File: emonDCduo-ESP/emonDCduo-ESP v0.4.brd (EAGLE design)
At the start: 99.1 x 76.5 mm, 78 parts, among them Q1 16Mhz XT49M-2016M, U1_TQFP ATMEGA328P

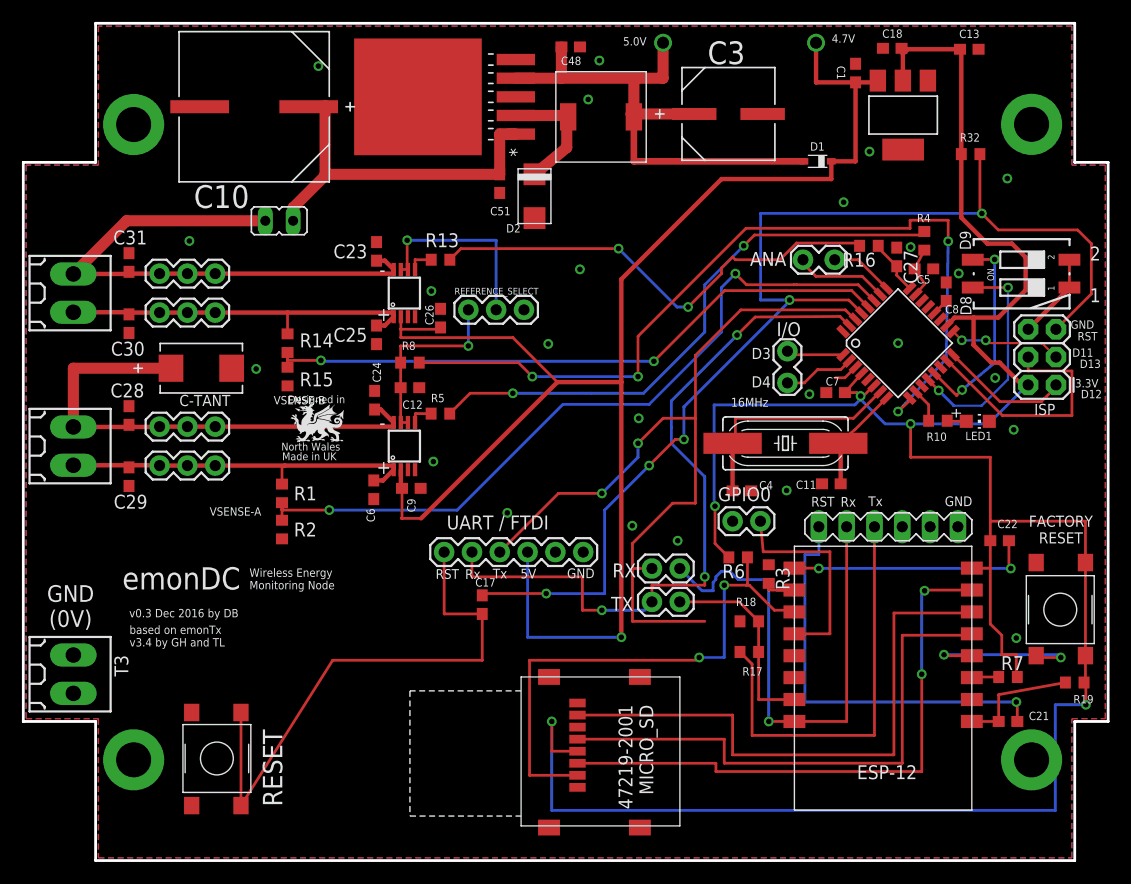
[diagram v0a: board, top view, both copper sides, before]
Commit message: RFM69 onto board
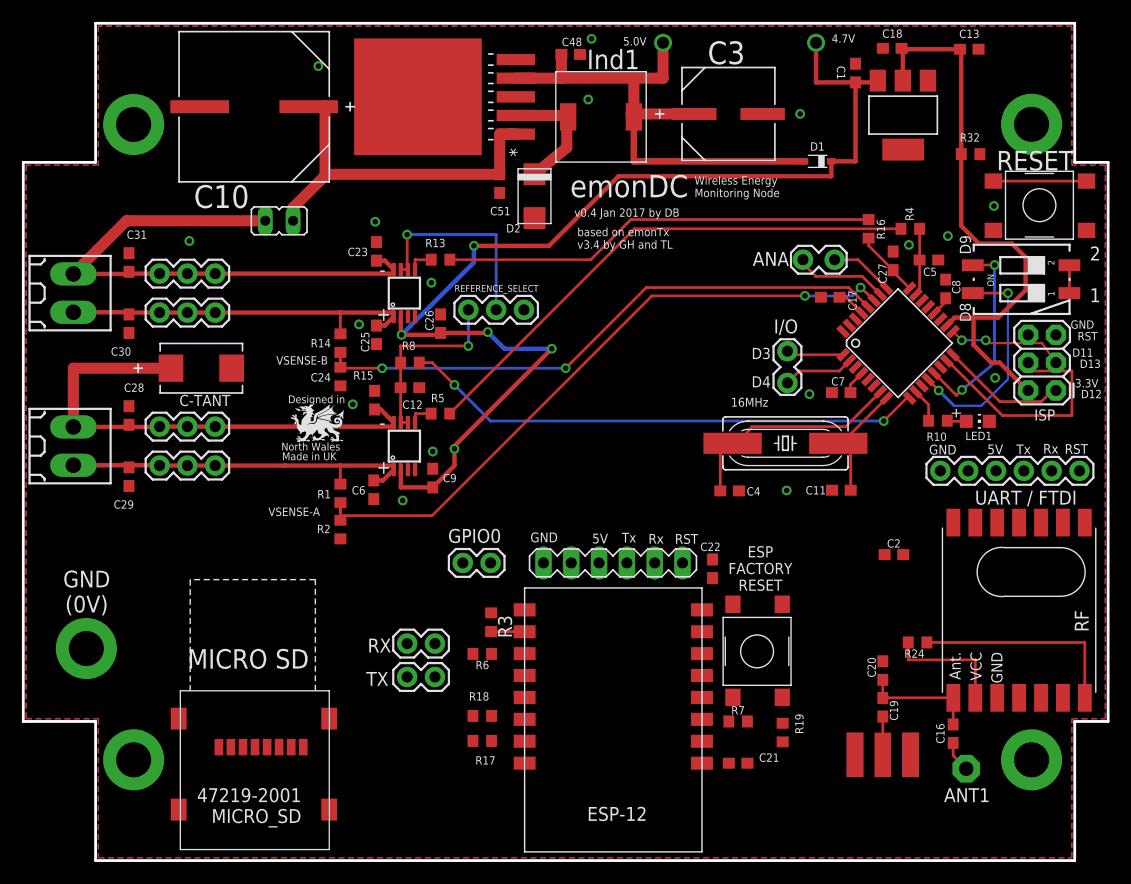
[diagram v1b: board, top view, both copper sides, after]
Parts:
- removed T3: (no value), con-weidmueller-sl35:180-2
- added ANT1: (no value), discrete:PAD-01
- added C16, C19: 22pF, rcl:C0603
- added C2: 100nF, rcl:C0603
- added C20: tune, rcl:C0603
- added J$1: SMA_EDGE, SparkFun-Connectors:SMA-EDGE
- added R24: 120K, rcl:R0603
- added RF: RFM12B, JeeParts:RFM12B
- C3: value 470UF -> 470uF
- moved MC32882 87.2 mm to (89.9, 58.5), turned to 0 degrees
- moved FTDI/UART 58.5 mm to (96.7, 37.4), turned to 180 degrees
- moved C17 42.4 mm to (73.9, 53.2), turned to 0 degrees
- moved MC1 27.9 mm to (70.4, 17.8)
- moved R19 27.1 mm to (69.6, 13.5), turned to 90 degrees
- moved C22 26.3 mm to (63.2, 28.4), turned to 270 degrees
- moved R18 25.9 mm to (42.2, 15.0)
- moved R3 25.7 mm to (43.0, 23.5)
- moved R17 25.7 mm to (42.2, 12.7)
- moved R6 25.0 mm to (42.2, 20.7)
- moved R7 25.0 mm to (65.5, 14.5)
- moved C21 24.9 mm to (65.5, 10.7)
- moved ESP-12 24.9 mm to (62.2, 26.7)
- moved GPIO0 24.9 mm to (40.4, 29.0)
- moved RX 23.4 mm to (37.8, 21.6)
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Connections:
- new net DIG1: C16.1, C19.1, C20.1, RF.ANT
- new net N$11: ANT1.1, C16.2
- new net N$24: C19.2, J$1.SIG
- net 3.3V: now also C2.1, R24.2, RF.VDD
- net D10: now also R24.1, RF.SEL
- net D11/MOSI: now also RF.SDI
- net D12/MISO: now also RF.SDO
- net D13/SCK: now also RF.SCK
- net D2: now also RF.IRQ
- net GND: now also C2.2, C20.2, J$1.GND@0, J$1.GND@1, J$1.GND@2, J$1.GND@3, RF.GND, RF.P$12; no longer T3.1, T3.2
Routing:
- net 3.3V: track 235.1 -> 66.2 mm, vias 5 -> 0
- net RESET: track 109.5 -> 2.63 mm, vias 5 -> 0
- net D0/RX: track 76.7 -> 0.00 mm, vias 2 -> 0
- net D1/TX: track 66.3 -> 0.00 mm, vias 3 -> 0
- net GPIO13: track 53.3 -> 0.00 mm, vias 2 -> 0
- net GPIO12: track 52.7 -> 0.00 mm
- net GPIO14: track 50.0 -> 0.00 mm
- net GPIO2: track 49.5 -> 0.00 mm, vias 2 -> 0
- net ESPTX: track 48.5 -> 0.00 mm, vias 1 -> 0
- net 4.7V: track 148.1 -> 104.2 mm, vias 2 -> 6
- net RES: track 52.0 -> 9.26 mm
- net N$30: track 38.4 -> 0.00 mm, vias 1 -> 0
- net N$36: track 38.3 -> 0.00 mm
- net D5/PWM0: track 78.3 -> 48.0 mm, vias 4 -> 2
- net GPIO15: track 27.1 -> 4.69 mm, vias 2 -> 0
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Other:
- board text added: "ESP FACTORY RESET"
- board text added: "Ind1"
- board text added: "MICRO SD"
- board text added: "v0.4 Jan 2017 by DB"
- board text removed: "FACTORY RESET"
- board text removed: "v0.3 Dec 2016 by DB"

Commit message: layout changes
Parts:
- moved RX 7.41 mm to (37.1, 14.2)
- moved ANA 1.78 mm to (72.4, 56.6)
- moved TX 1.70 mm to (37.1, 17.0)
- moved GPIO0 1.63 mm to (41.7, 27.9)
- moved FTDI/UART 1.27 mm to (95.4, 37.4)
- moved C2 0.51 mm to (79.8, 30.2)
- moved C17 0.34 mm to (73.9, 52.9)
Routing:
- net 3.3V: track 66.2 -> 269.4 mm, vias 0 -> 6
- net D0/RX: track 0.00 -> 93.7 mm, vias 0 -> 3
- net D1/TX: track 0.00 -> 86.1 mm, vias 0 -> 4
- net 4.7V: track 104.2 -> 167.9 mm, vias 6 -> 8
- net GPIO13: track 0.00 -> 63.0 mm, vias 0 -> 2
- net RES: track 9.26 -> 64.3 mm, vias 0 -> 3
- net GPIO14: track 0.00 -> 54.8 mm
- net GPIO12: track 0.00 -> 52.5 mm
- net GPIO2: track 0.00 -> 50.5 mm, vias 0 -> 2
- net D10: track 19.6 -> 67.7 mm, vias 0 -> 4
- net RESET: track 2.63 -> 49.1 mm, vias 0 -> 2
- net ESPTX: track 0.00 -> 42.7 mm, vias 0 -> 1
- net D2: track 0.00 -> 41.3 mm, vias 0 -> 2
- net D13/SCK: track 11.0 -> 45.2 mm, vias 2 -> 5
- net N$36: track 0.00 -> 33.7 mm, vias 0 -> 1
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
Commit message: DRC edited
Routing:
- net GPIO13: track 63.0 -> 64.9 mm
- net D12/MISO: track 26.4 -> 27.9 mm
- net GPIO2: track 50.5 -> 50.0 mm
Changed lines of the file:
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@@
 <rectangle x1="50.109509375" y1="16.957528125" x2="52.101309375" y2="19.025528125" layer="122" rot="R180"/>
 <text x="74.295" y="17.145" size="1.778" layer="112" font="vector" ratio="10"></text>
-<text x="50.5642" y="60.5648" size="0.762" layer="112" font="vector" ratio="15">v0.4 Jan 2017 by DB</text>
-<text x="50.1844" y="62.343" size="2.032" layer="112" font="vector" ratio="15">emonDC</text>
+<text x="10.4322" y="26.5288" size="0.762" layer="112" font="vector" ratio="15">v0.4 Jan 2017 by DB</text>
+<text x="10.0524" y="28.307" size="2.032" layer="112" font="vector" ratio="15">emonDC</text>
 <text x="26.2382" y="12.0142" size="1.016" layer="22" font="vector" ratio="15" rot="MR0">Open-Hardware</text>
 <text x="24.432340625" y="43.539921875" size="0.7112" layer="121" font="vector" ratio="15" rot="SR0">Designed in </text>
@@
 <rectangle x1="91.710159375" y1="63.837721875" x2="91.805359375" y2="63.844121875" layer="22" rot="R180"/>
 <rectangle x1="91.297359375" y1="63.837721875" x2="91.341859375" y2="63.844121875" layer="22" rot="R180"/>
-<text x="61.5446" y="62.3594" size="0.762" layer="112" font="vector" ratio="15">Wireless Energy
+<text x="21.4126" y="28.3234" size="0.762" layer="112" font="vector" ratio="15">Wireless Energy
 Monitoring Node</text>
 <text x="62.865" y="33.401" size="1.4224" layer="122" rot="MR0">SMT V0.6 rev3</text>
@@
 <wire x1="6.858" y1="78.232" x2="96.266" y2="78.232" width="0.254" layer="20"/>
 <wire x1="100" y1="80" x2="100" y2="0" width="0.05" layer="157"/>
-<text x="50.8428" y="57.6492" size="0.762" layer="112" font="vector" ratio="15">based on emonTx
+<text x="10.7108" y="23.6132" size="0.762" layer="112" font="vector" ratio="15">based on emonTx
 v3.4 by GH and TL</text>
 <text x="74.0766" y="76.4598" size="0.762" layer="112" font="vector" ratio="15">4.7V</text>
@@
 <via x="86.7134" y="29.3402" extent="1-16" drill="0.5"/>
 <via x="80.1602" y="49.0252" extent="1-16" drill="0.5"/>
+<wire x1="28.194" y1="6.432" x2="28.304" y2="11.442" width="0" layer="19" extent="1-1"/>
 </signal>
 <signal name="ADCVSENSE-A">
@@
 <wire x1="95.25" y1="35.306" x2="81.28" y2="35.306" width="0.254" layer="16"/>
 <wire x1="81.28" y1="35.306" x2="81.28" y2="40.386" width="0.254" layer="16"/>
-<wire x1="81.28" y1="40.386" x2="72.898" y2="49.022" width="0.254" layer="16"/>
-<via x="72.898" y="49.022" extent="1-16" drill="0.5"/>
-<wire x1="72.898" y1="49.022" x2="73.953425" y2="50.077425" width="0.254" layer="1"/>
+<wire x1="81.28" y1="40.386" x2="72.7456" y2="48.9204" width="0.254" layer="16"/>
+<via x="72.7456" y="48.9204" extent="1-16" drill="0.5"/>
+<wire x1="72.7456" y1="48.9204" x2="73.953425" y2="50.077425" width="0.254" layer="1"/>
 <wire x1="73.953425" y1="50.077425" x2="75.121771875" y2="50.077425" width="0.254" layer="1"/>
 </signal>
@@
 <wire x1="84.5865375" y1="47.400884375" x2="84.552115625" y2="47.400884375" width="0.2032" layer="1"/>
 <wire x1="84.552115625" y1="47.400884375" x2="84.5312" y2="47.4726" width="0.2032" layer="1"/>
-<wire x1="92.012" y1="47.244" x2="92.012" y2="46.482" width="0.254" layer="1"/>
-<wire x1="92.012" y1="46.482" x2="96.012" y2="46.482" width="0.254" layer="1"/>
+<wire x1="92.012" y1="47.244" x2="92.012" y2="45.9994" width="0.254" layer="1"/>
+<wire x1="92.012" y1="45.9994" x2="96.012" y2="45.9994" width="0.254" layer="1"/>
 <wire x1="84.5865375" y1="47.400884375" x2="84.679115625" y2="47.400884375" width="0.254" layer="1"/>
 <wire x1="84.679115625" y1="47.400884375" x2="89.662" y2="42.418" width="0.254" layer="1"/>
 <wire x1="89.662" y1="42.418" x2="94.996" y2="42.418" width="0.254" layer="1"/>
 <wire x1="94.996" y1="42.418" x2="96.012" y2="42.418" width="0.254" layer="1"/>
-<wire x1="96.012" y1="42.418" x2="96.012" y2="46.482" width="0.254" layer="1"/>
+<wire x1="96.012" y1="42.418" x2="96.012" y2="45.9994" width="0.254" layer="1"/>
 <contactref element="RF" pad="SDI"/>
 <wire x1="93.186" y1="16.638" x2="93.218" y2="16.67" width="0.254" layer="1"/>
@@
 <contactref element="ISP" pad="1"/>
 <wire x1="85.1052625" y1="48.038934375" x2="85.152225" y2="47.966571875" width="0.2032" layer="1"/>
-<wire x1="85.152225" y1="47.966571875" x2="89.430796875" y2="43.688" width="0.254" layer="1"/>
-<wire x1="89.430796875" y1="43.688" x2="93.218" y2="43.688" width="0.254" layer="1"/>
-<wire x1="93.218" y1="43.688" x2="94.552" y2="45.022" width="0.254" layer="1"/>
+<wire x1="85.152225" y1="47.966571875" x2="89.938796875" y2="43.18" width="0.254" layer="1"/>
+<wire x1="89.938796875" y1="43.18" x2="94.5642" y2="43.18" width="0.254" layer="1"/>
+<wire x1="94.5642" y1="43.18" x2="94.552" y2="45.022" width="0.254" layer="1"/>
 <wire x1="94.552" y1="45.022" x2="94.552" y2="44.704" width="0.254" layer="1"/>
 <contactref element="RF" pad="SDO"/>
@@
 <via x="88.141" y="49.284" extent="1-16" drill="0.5"/>
 <wire x1="88.141" y1="49.284" x2="88.259" y2="49.029" width="0.2032" layer="1"/>
-<wire x1="88.259" y1="49.029" x2="88.206" y2="49.032" width="0.2032" layer="1"/>
-<wire x1="88.206" y1="49.032" x2="93.282" y2="49.022" width="0.2032" layer="1"/>
-<wire x1="93.282" y1="49.022" x2="94.552" y2="47.244" width="0.2032" layer="1"/>
+<wire x1="88.259" y1="49.029" x2="88.7394" y2="48.524" width="0.2032" layer="1"/>
+<wire x1="88.7394" y1="48.524" x2="93.8154" y2="48.514" width="0.2032" layer="1"/>
+<wire x1="93.8154" y1="48.514" x2="94.552" y2="47.244" width="0.2032" layer="1"/>
 <wire x1="85.1052625" y1="49.9796625" x2="85.152225" y2="50.077425" width="0.2032" layer="1"/>
 <contactref element="RF" pad="SCK"/>
@@
 <wire x1="82.1042" y1="59.4664" x2="82.1042" y2="56.6238" width="0.254" layer="1"/>
 <wire x1="82.1042" y1="56.6238" x2="82.1002" y2="56.6198" width="0.254" layer="1"/>
-<wire x1="82.1002" y1="56.6198" x2="82.1002" y2="53.813625" width="0.254" layer="1"/>
-<wire x1="82.1002" y1="53.813625" x2="81.7581125" y2="53.4715375" width="0.254" layer="1"/>
+<wire x1="82.296" y1="54.009425" x2="81.7581125" y2="53.4715375" width="0.254" layer="1"/>
+<wire x1="82.296" y1="54.009425" x2="82.296" y2="56.6198" width="0.254" layer="1"/>
+<wire x1="82.296" y1="56.6198" x2="82.1002" y2="56.6198" width="0.254" layer="1"/>
 </signal>
 <signal name="N$6">
@@
 <contactref element="U1_TQFP" pad="9"/>
 <wire x1="81.0692625" y1="44.155334375" x2="81.192425" y2="44.006771875" width="0.2032" layer="1"/>
-<wire x1="81.0692625" y1="44.155334375" x2="78.823928125" y2="41.91" width="0.254" layer="1"/>
-<wire x1="78.823928125" y1="41.91" x2="42.926" y2="41.91" width="0.254" layer="16"/>
+<wire x1="81.0692625" y1="44.155334375" x2="78.671528125" y2="41.8084" width="0.254" layer="1"/>
+<wire x1="78.671528125" y1="41.8084" x2="42.926" y2="41.91" width="0.254" layer="16"/>
 <wire x1="42.926" y1="41.91" x2="39.624" y2="45.212" width="0.254" layer="16"/>
 <via x="39.624" y="45.212" extent="1-16" drill="0.5"/>
 <wire x1="39.624" y1="45.212" x2="37.592" y2="47.244" width="0.254" layer="1"/>
 <wire x1="37.592" y1="47.244" x2="36.41" y2="47.244" width="0.254" layer="1"/>
-<via x="78.823928125" y="41.91" extent="1-16" drill="0.5"/>
+<via x="78.671528125" y="41.8084" extent="1-16" drill="0.5"/>
 </signal>
 <signal name="N$19">
@@
 <contactref element="U$1" pad="PIN2"/>
 <contactref element="R6" pad="1"/>
-<wire x1="19.214" y1="12.132" x2="19.214" y2="4.572" width="0.254" layer="1"/>
-<wire x1="19.214" y1="4.572" x2="42.926" y2="4.572" width="0.254" layer="1"/>
-<via x="42.926" y="4.572" extent="1-16" drill="0.5"/>
-<wire x1="42.926" y1="4.572" x2="42.926" y2="18.034" width="0.254" layer="16"/>
+<wire x1="19.214" y1="12.132" x2="19.214" y2="4.826" width="0.254" layer="1"/>
+<via x="42.926" y="6.604" extent="1-16" drill="0.5"/>
+<wire x1="42.926" y1="6.604" x2="42.926" y2="18.034" width="0.254" layer="16"/>
 <via x="42.926" y="18.034" extent="1-16" drill="0.5"/>
 <wire x1="42.926" y1="18.034" x2="42.926" y2="20.6502" width="0.254" layer="1"/>
@@
 <wire x1="43.014" y1="20.6502" x2="43.0338" y2="20.67" width="0.254" layer="1"/>
 <wire x1="43.0338" y1="20.67" x2="46.03" y2="20.67" width="0.254" layer="1"/>
+<wire x1="42.926" y1="6.604" x2="42.926" y2="4.826" width="0.254" layer="1"/>
+<wire x1="42.926" y1="4.826" x2="19.214" y2="4.826" width="0.254" layer="1"/>
 </signal>
 <signal name="GPIO5">
@@
 <wire x1="20.314" y1="6.858" x2="25.908" y2="6.858" width="0.254" layer="1"/>
 <via x="25.908" y="6.858" extent="1-16" drill="0.5"/>
-<wire x1="25.908" y1="6.858" x2="56.642" y2="6.858" width="0.254" layer="16"/>
-<wire x1="56.642" y1="6.858" x2="56.642" y2="22.606" width="0.254" layer="16"/>
+<wire x1="56.642" y1="5.588" x2="56.642" y2="22.606" width="0.254" layer="16"/>
 <via x="56.642" y="22.606" extent="1-16" drill="0.5"/>
 <wire x1="56.642" y1="22.606" x2="62.23" y2="22.606" width="0.254" layer="1"/>
 <wire x1="62.23" y1="22.606" x2="62.23" y2="22.67" width="0.4064" layer="1"/>
+<wire x1="25.908" y1="6.858" x2="25.908" y2="6.604" width="0.254" layer="16"/>
+<wire x1="25.908" y1="6.604" x2="41.148" y2="6.604" width="0.254" layer="16"/>
+<wire x1="41.148" y1="6.604" x2="42.164" y2="5.588" width="0.254" layer="16"/>
+<wire x1="42.164" y1="5.588" x2="56.642" y2="5.588" width="0.254" layer="16"/>
 </signal>
 <signal name="N$7">

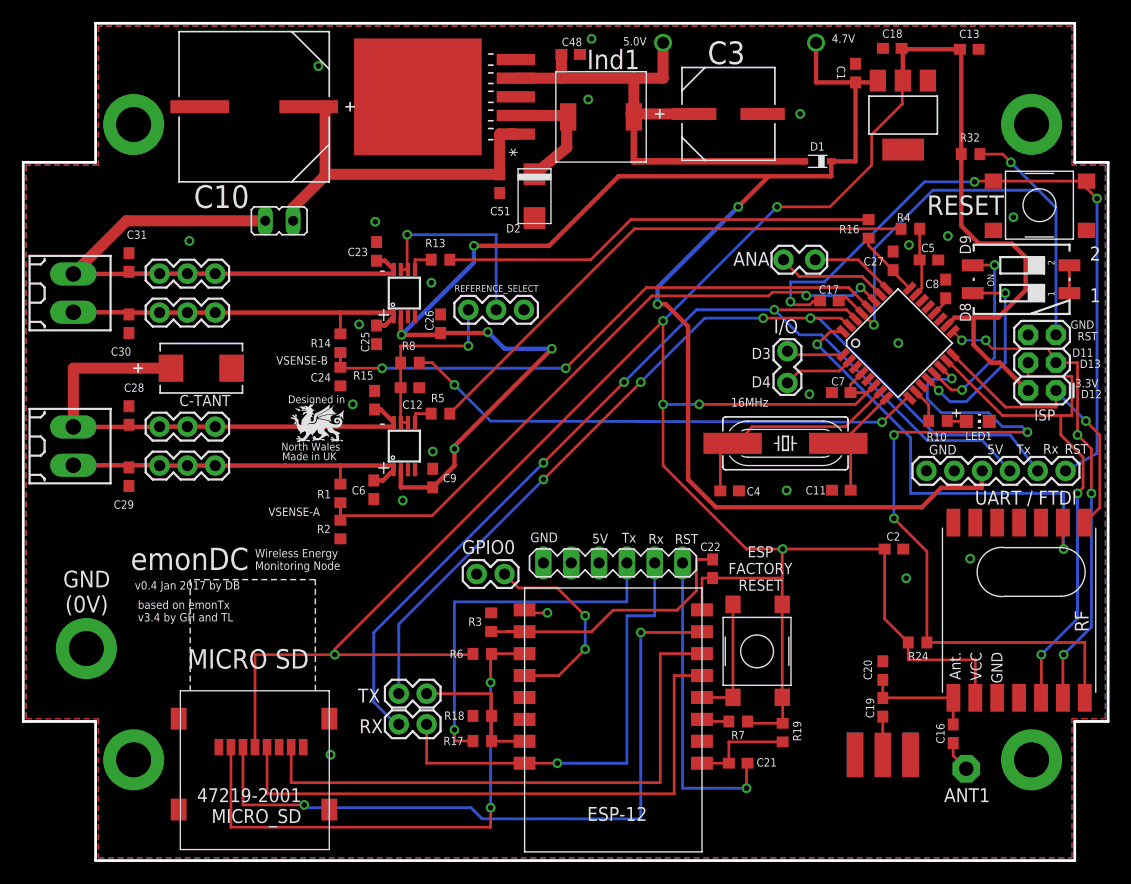
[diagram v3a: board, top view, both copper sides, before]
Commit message: antenna caps removed. camexport
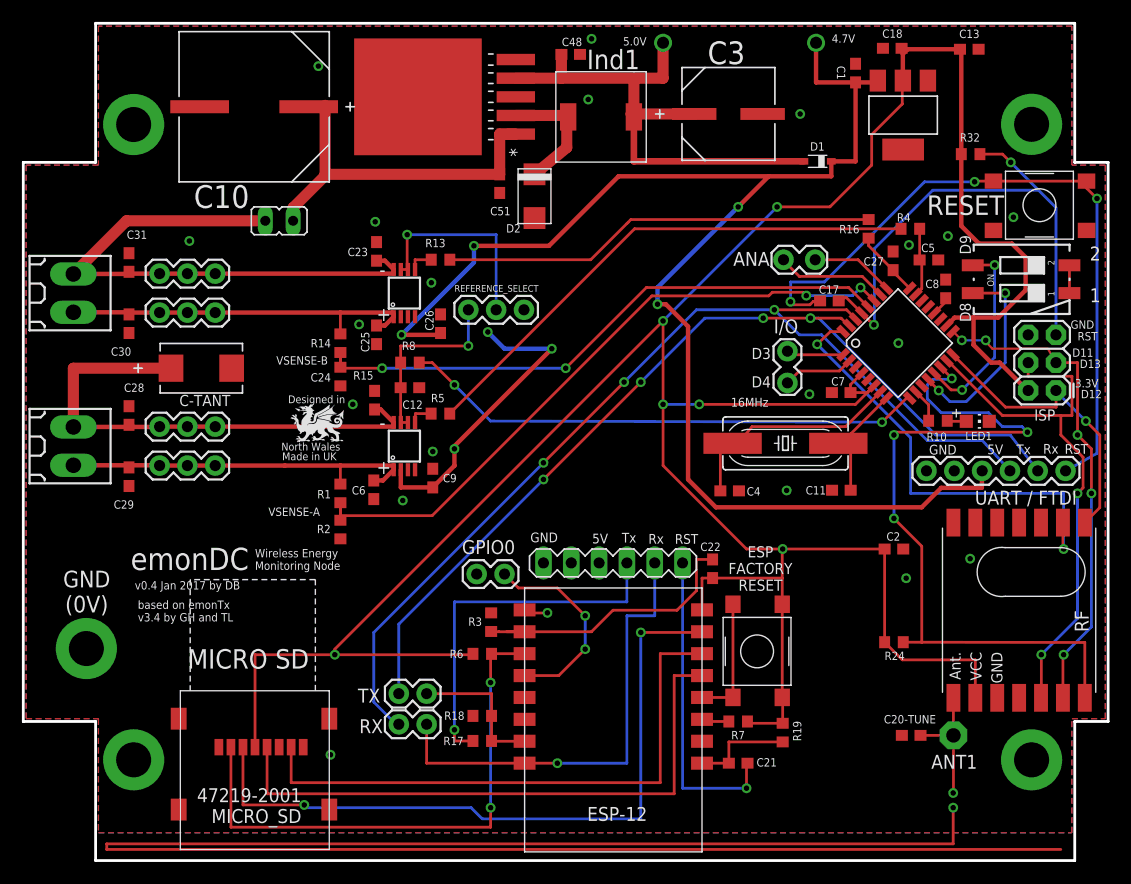
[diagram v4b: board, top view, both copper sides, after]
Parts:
- removed C16, C19: 22pF, rcl:C0603
- removed C20: tune, rcl:C0603
- removed J$1: SMA_EDGE, SparkFun-Connectors:SMA-EDGE
- added C20-TUNE: tune, rcl:C0603
- moved ANT1 3.26 mm to (85.2, 13.2)
- moved R24 2.16 mm to (79.8, 21.7)
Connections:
- removed net N$11: ANT1.1, C16.2
- removed net N$24: C19.2, J$1.SIG
- net DIG1: now also ANT1.1, C20-TUNE.1; no longer C16.1, C19.1, C20.1
- net GND: now also C20-TUNE.2; no longer C20.2, J$1.GND@0, J$1.GND@1, J$1.GND@2, J$1.GND@3
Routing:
- net N$31: track 0.00 -> 168.2 mm, vias 0 -> 1
- net 4.7V: track 167.9 -> 161.7 mm
- net N$24: track 3.49 -> 0.00 mm
- net N$11: track 2.84 -> 0.00 mm
- net D10: track 67.7 -> 69.7 mm
- net DIG1: track 10.6 -> 11.9 mm, vias 0 -> 1
